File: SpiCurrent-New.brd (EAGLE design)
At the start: 445.8 x 364.2 mm, 58 parts, among them IC1 AD822N, IC2 AD822N, IC3 ACS758LCB-050B-PFF-T, IC4 ACS758LCB-050B-PFF-T, U1 HIP4081AIPZ

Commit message: Grossly laid out; still need to check (C5 is weird), check traces, adjust trace widths etc
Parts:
- added C9: 0.1uf, rcl:C050-055X075
- moved H8 307.8 mm to (20.3, 188.0)
- moved H6 236.2 mm to (167.6, 188.0)
- moved JP1 158.4 mm to (40.6, 63.5), turned to 270 degrees
- moved H1 150.0 mm to (91.4, 101.6), turned to 270 degrees
- moved H5 138.6 mm to (20.3, 15.2)
- moved H3 127.0 mm to (106.7, 95.2)
- moved C7 123.8 mm to (163.8, 106.7), turned to 180 degrees
- moved U$1 122.1 mm to (39.4, 78.7), turned to 180 degrees
- moved C5 118.4 mm to (152.4, 106.7), turned to 0 degrees
- moved H2 115.7 mm to (121.9, 101.6), turned to 180 degrees
- moved R14 103.1 mm to (168.9, 114.3), turned to 90 degrees
- moved D3 93.6 mm to (81.3, 179.1), turned to 270 degrees
- moved R3 93.2 mm to (83.8, 181.6), turned to 270 degrees
- moved H4 81.4 mm to (106.7, 110.5)
- moved IC4 80.0 mm to (144.8, 118.1), turned to 90 degrees
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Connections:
- net +5V: now also C9.1
- net GND: now also C9.2
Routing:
- net +12V: track 545.4 -> 274.3 mm
- net +5V: track 478.8 -> 339.2 mm, vias 0 -> 1
- net N$7: track 64.9 -> 189.2 mm
- net N$3: track 21.4 -> 121.9 mm
- net N$5: track 88.4 -> 177.8 mm, vias 1 -> 0
- net N$24: track 92.6 -> 17.8 mm
- net N$32: track 274.3 -> 340.4 mm
- net N$11: track 218.5 -> 154.4 mm
- net N$25: track 80.6 -> 22.9 mm
- net N$4: track 60.2 -> 10.2 mm
- net N$33: track 255.6 -> 298.4 mm
- net N$14: track 182.1 -> 139.4 mm
- net N$16: track 156.1 -> 130.2 mm
- net N$36: track 34.2 -> 11.4 mm
- net N$9: track 104.9 -> 127.0 mm
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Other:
- board size 445.8 x 364.2 mm -> 162.6 x 188 mm

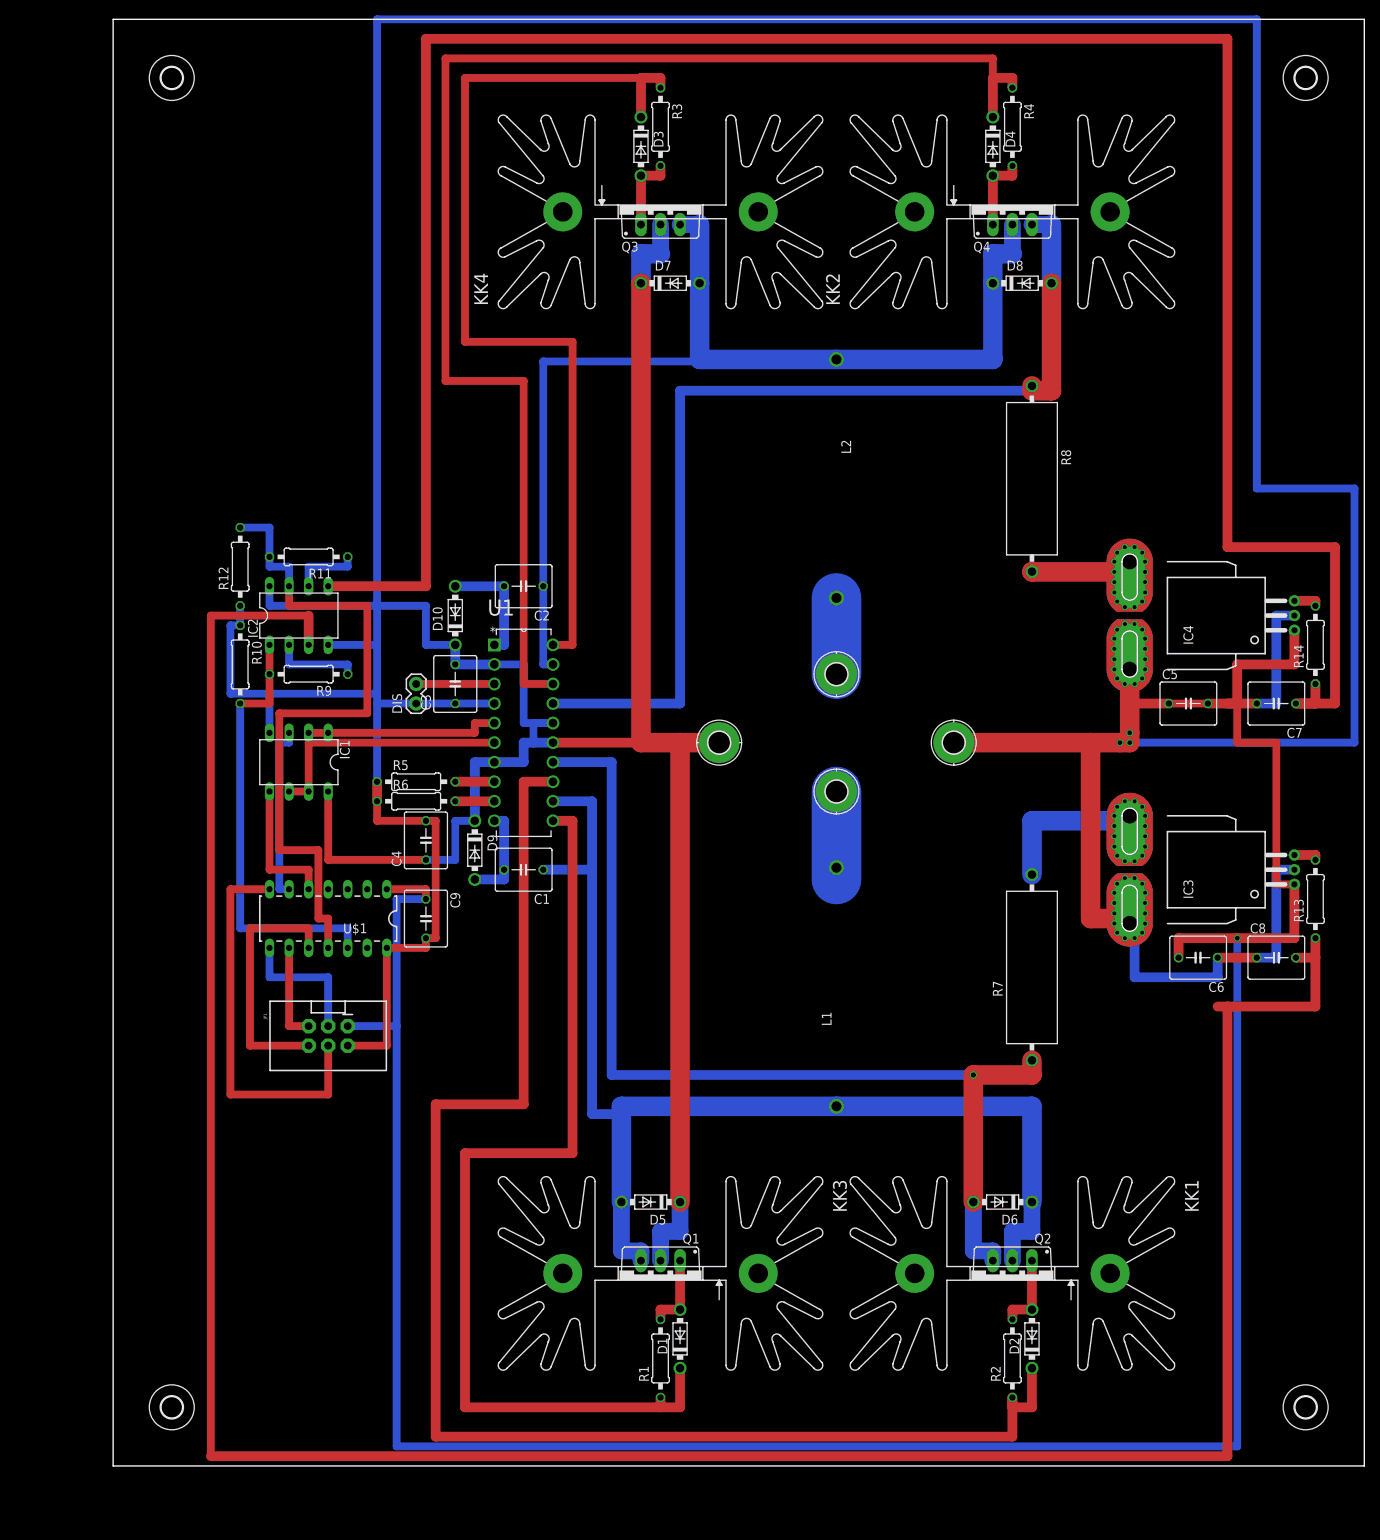
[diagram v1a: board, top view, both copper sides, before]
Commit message: Layout complete. NB fancy mask stuff is NOT complete, use this one for low(ish) current testing
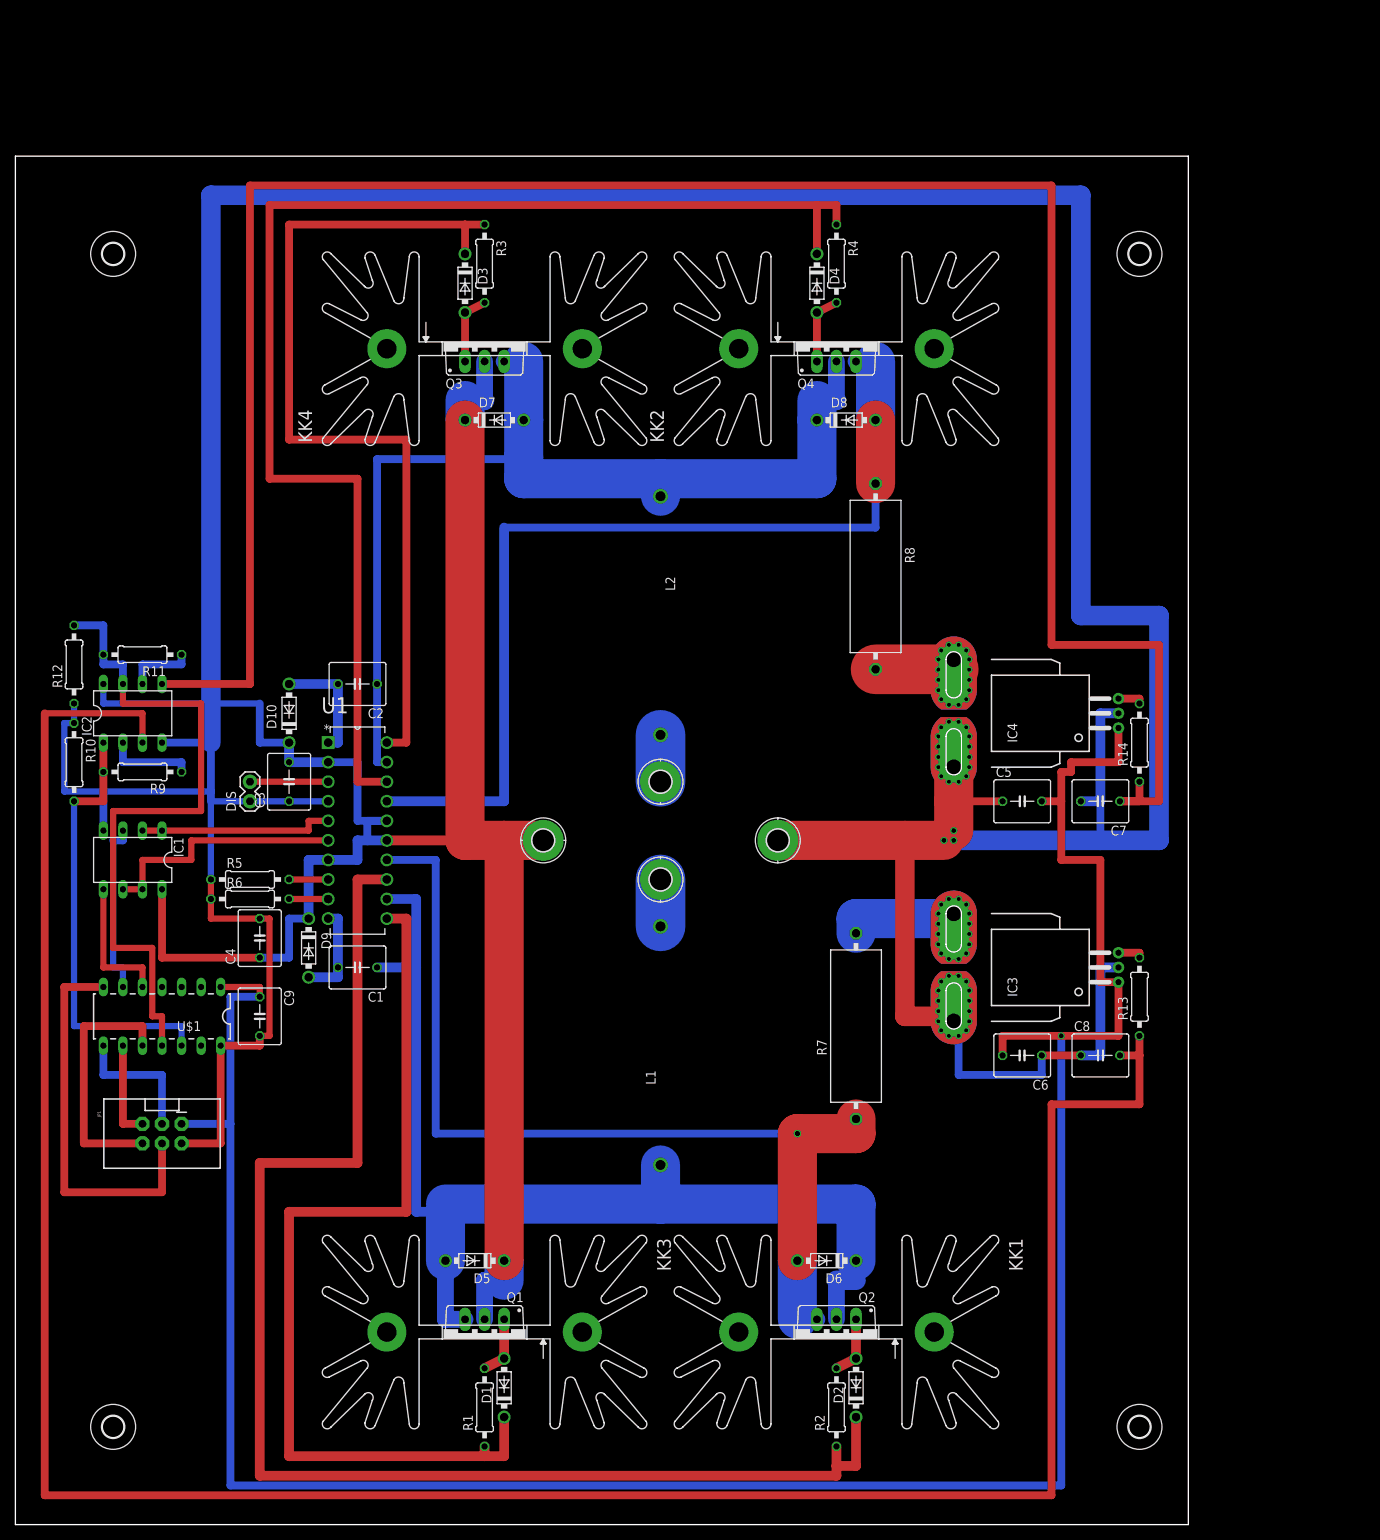
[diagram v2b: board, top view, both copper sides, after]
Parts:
- moved H6 31.4 mm to (146.1, 165.1)
- moved D7 29.0 mm to (62.2, 143.5)
- moved L2 29.0 mm to (83.8, 118.1)
- moved D3 29.0 mm to (58.4, 161.3)
- moved D4 29.0 mm to (104.1, 161.3)
- moved D8 29.0 mm to (108.0, 143.5)
- moved KK4 29.0 mm to (61.0, 153.7)
- moved Q3 29.0 mm to (61.0, 153.7)
- moved R3 29.0 mm to (61.0, 163.8)
- moved KK2 29.0 mm to (106.7, 153.7)
- moved Q4 29.0 mm to (106.7, 153.7)
- moved R4 29.0 mm to (106.7, 163.8)
- moved H4 26.8 mm to (83.8, 96.5)
- moved C7 26.2 mm to (141.0, 94.0)
- moved C8 26.2 mm to (141.0, 61.0)
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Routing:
- net GND: track 617.5 -> 587.0 mm
- net +5V: track 339.2 -> 321.4 mm
- net N$32: track 340.4 -> 322.6 mm
- net N$33: track 298.4 -> 284.5 mm
- net +12V: track 274.3 -> 262.9 mm
- net N$7: track 189.2 -> 181.6 mm
- net N$11: track 154.4 -> 146.8 mm
- net N$3: track 121.9 -> 114.3 mm
- net N$16: track 130.2 -> 123.2 mm
- net N$15: track 131.4 -> 125.1 mm
- net N$36: track 11.4 -> 6.09 mm
- net N$5: track 177.8 -> 172.7 mm
- net N$9: track 127.0 -> 121.9 mm
- net N$31: track 19.7 -> 14.6 mm
- net N$37: track 9.90 -> 6.09 mm
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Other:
- board size 162.6 x 188 mm -> 152.4 x 177.8 mm
